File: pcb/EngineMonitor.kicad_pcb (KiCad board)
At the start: 2 copper layers, 71 parts, among them K1 CONN_3, K2 CONN_3, K3 CONN_3, K4 CONN_3, P1 CONN_6, P2 CONN_6, P3 CONN_1, P4 CONN_1, P5 CONN_4, P6 CONN_4, P7 CONN_4, U1 74HC14, U2 ESP32Dev

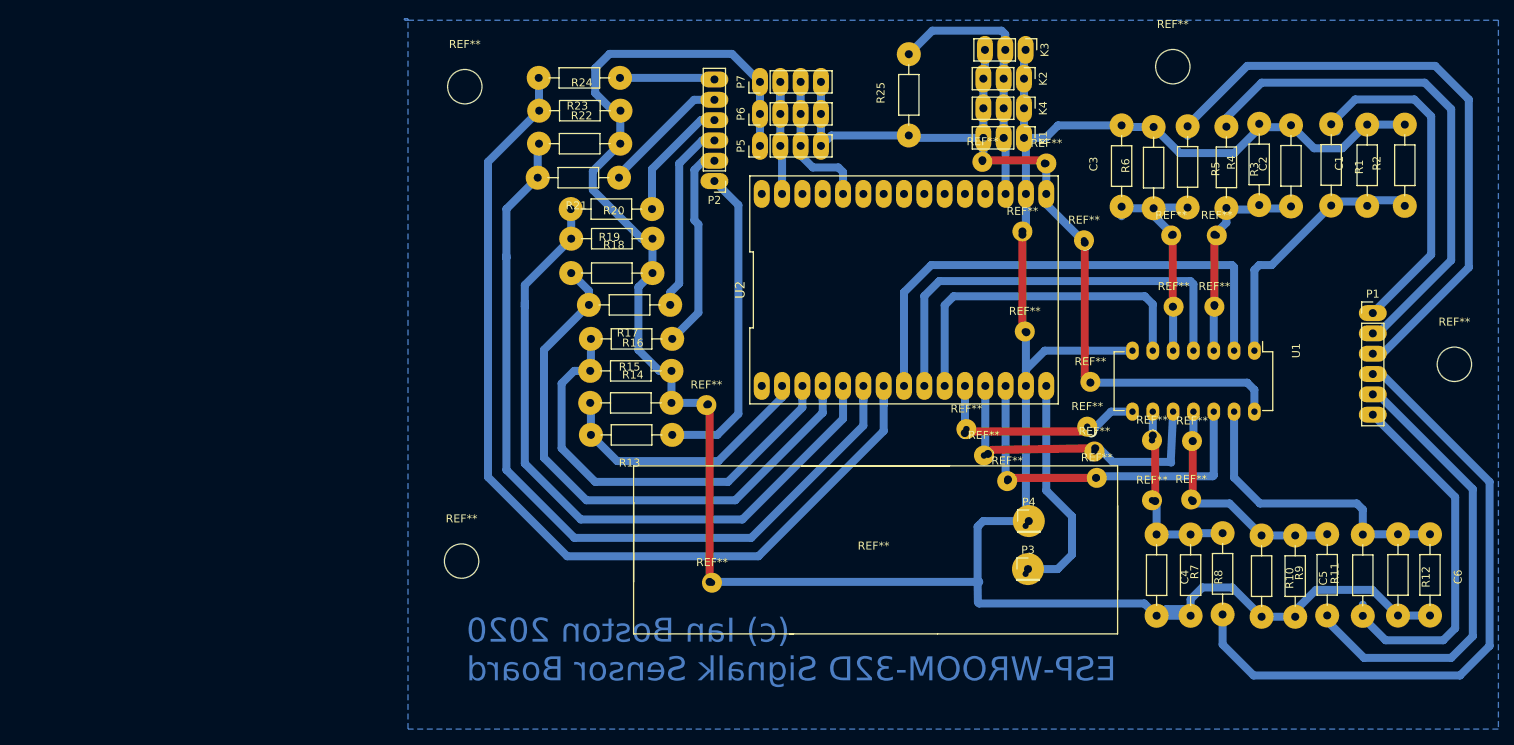
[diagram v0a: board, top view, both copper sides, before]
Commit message: Redisigned board and fixed sensors
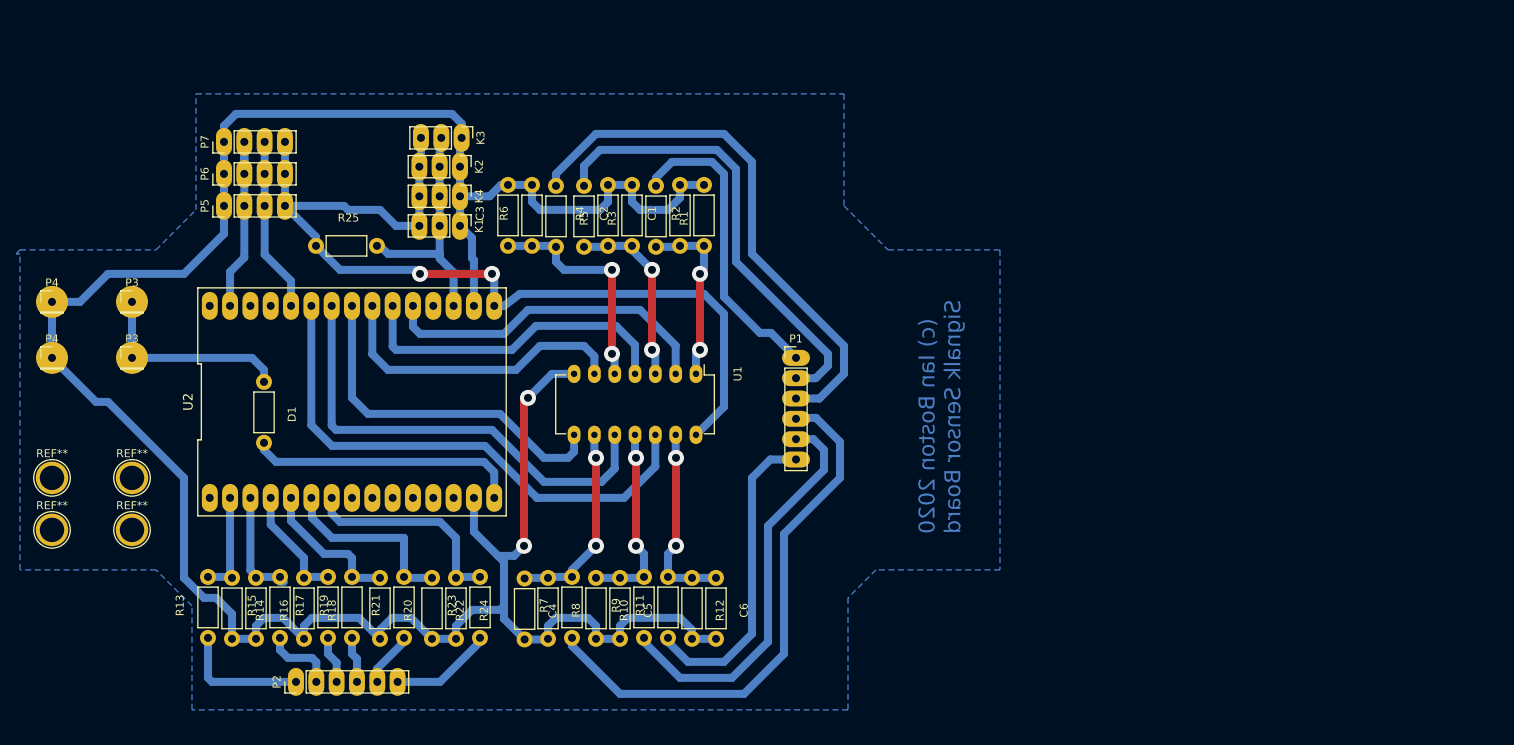
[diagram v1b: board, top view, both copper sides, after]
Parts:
- removed the REF** at (144.7, 137.5)
- removed the REF** at (187.3, 107.1)
- removed the REF** at (182.2, 107.1)
- removed the REF** at (163.6, 110.2)
- removed the REF** at (171.8, 116.5)
- removed the REF** at (166.3, 89.2)
- removed the REF** at (158.3, 89.0)
- removed the REF** at (123.8, 119.4)
- removed the REF** at (124.5, 141.6)
- removed the REF** at (156.3, 122.4)
- removed the REF** at (158.5, 125.7)
- removed the REF** at (93.6, 79.6)
- removed the REF** at (161.4, 128.9)
- removed the REF** at (172.6, 128.5)
- removed the REF** at (172.3, 125.2)
- removed the REF** at (171.4, 122.1)
- removed the REF** at (179.5, 123.8)
- removed the REF** at (179.5, 131.3)
- removed the REF** at (184.4, 131.2)
- removed the REF** at (184.5, 123.9)
- removed the REF** at (93.2, 138.9)
- removed the REF** at (182.1, 77.1)
- removed the REF** at (217.3, 114.3)
- removed the REF** at (171.0, 98.8)
- removed the REF** at (163.3, 97.7)
- removed the REF** at (181.9, 98.2)
- removed the REF** at (187.6, 98.2)
- added D1: DIODE, Resistors_ThroughHole:Resistor_Horizontal_RM7mm, F.Cu at (68.5, 116.5)
- added P3: CONN_1, Pin_Headers:Pin_Header_Straight_1x01_Pitch2.54mm, F.Cu at (52.0, 106.5)
- added P4: CONN_1, Pin_Headers:Pin_Header_Straight_1x01_Pitch2.54mm, F.Cu at (42.0, 106.5)
- added REF**: 1pin, Connect:1pin, F.Cu at (42.0, 135.0)
- added REF**: 1pin, Connect:1pin, F.Cu at (52.0, 135.0)
- added REF**: 1pin, Connect:1pin, F.Cu at (52.0, 128.5)
- added REF**: 1pin, Connect:1pin, F.Cu at (42.0, 128.5)
- C1, C2, C3, C4, C5, C6, R1, R10, R11, R12, R13, R14, R15, R16, R17, R18, R19, R2, R20, R21, R22, R23, R24, R25, R3, R4, R5, R6, R7, R8, R9: footprint Resistors_ThroughHole:Resistor_Horizontal_RM10mmLargePads -> Resistors_ThroughHole:Resistor_Horizontal_RM7mm
- moved P4 123.8 mm to (42.0, 113.5)
- moved P3 115.1 mm to (52.0, 113.5)
- moved C6 89.4 mm to (125.0, 141.0)
- moved R12 88.4 mm to (122.0, 141.0)
- moved R2 87.7 mm to (123.5, 99.5)
- moved R11 86.9 mm to (119.0, 148.5)
- moved C1 86.0 mm to (120.5, 99.5)
- moved R9 85.4 mm to (116.0, 148.5)
- moved R1 84.8 mm to (117.5, 92.0)
- moved C5 84.6 mm to (113.0, 141.0)
- moved R10 83.4 mm to (110.0, 141.0)
- moved C2 82.5 mm to (114.5, 99.5)
- moved P2 81.6 mm to (72.5, 154.0), turned to 90 degrees
- moved R4 81.6 mm to (111.5, 99.5)
- moved R7 81.4 mm to (107.0, 148.5)
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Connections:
- P3 pad 1: 5v -> Net-(D1-Pad1)
- U2 pad 10: DIN3 -> (no net)
- U2 pad 11: DIN4 -> (no net)
- U2 pad 12: DIN5 -> (no net)
- U2 pad 13: DIN6 -> (no net)
- U2 pad 20: (no net) -> DIN1
- U2 pad 21: (no net) -> DIN2
- U2 pad 22: (no net) -> DIN3
- U2 pad 23: (no net) -> DIN4
- U2 pad 24: (no net) -> DIN5
- U2 pad 25: (no net) -> DIN6
- U2 pad 8: DIN1 -> (no net)
- U2 pad 9: DIN2 -> (no net)
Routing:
- net Net-(R23-Pad2): track 121.2 -> 26.6 mm
- net Net-(R21-Pad2): track 103.6 -> 23.5 mm
- net Net-(R19-Pad2): track 89.0 -> 18.3 mm
- net Net-(R17-Pad2): track 73.0 -> 14.5 mm
- net GND: track 369.8 -> 319.0 mm, vias 4 -> 2
- net Net-(R15-Pad2): track 56.3 -> 13.6 mm
- net Net-(D1-Pad1): track 0.00 -> 25.6 mm
- net Net-(P2-Pad1): track 41.1 -> 16.2 mm
- net DIN6: track 45.7 -> 67.3 mm, vias 2 -> 0
- net Net-(R13-Pad2): track 34.0 -> 12.6 mm
- net DIN1: track 64.9 -> 44.1 mm
- net DIN5: track 38.8 -> 58.2 mm, vias 2 -> 0
- net DIN4: track 28.0 -> 44.8 mm, vias 2 -> 0
- net Net-(P2-Pad2): track 26.4 -> 9.64 mm
- net Net-(P2-Pad3): track 23.7 -> 7.41 mm
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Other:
- board text added: "(c) Ian Boston 2020 Signalk Sensor Board"
- board text removed: "(c) Ian Boston 2020 ESP-WROOM-32D Signalk Sensor Board"
